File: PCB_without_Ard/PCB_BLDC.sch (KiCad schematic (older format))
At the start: 72 parts, among them J1 Ground Terminal, J2 Conn_01x03, J3 Conn_01x05, J4 Conn_01x02, J5 Conn_01x04, J6 Conn_01x04, J7 Conn_01x04, J8 Power Terminal, J9 Conn_01x02, Q1 IRF4905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

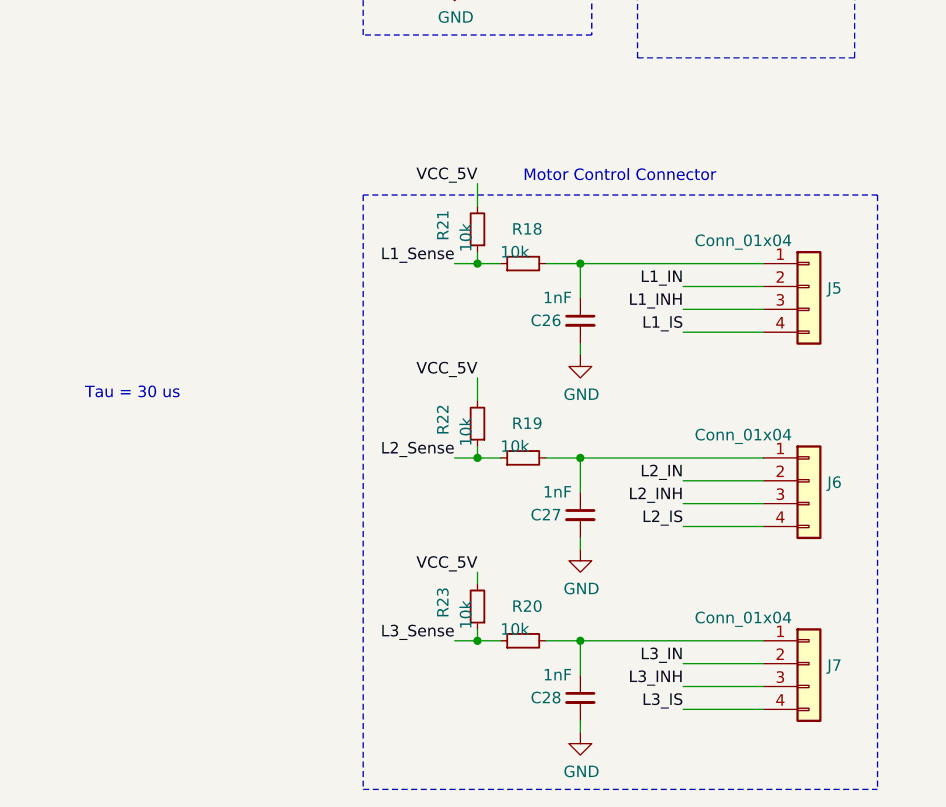
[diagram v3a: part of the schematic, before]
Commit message: Remove RC-Filter for Hall Sensors
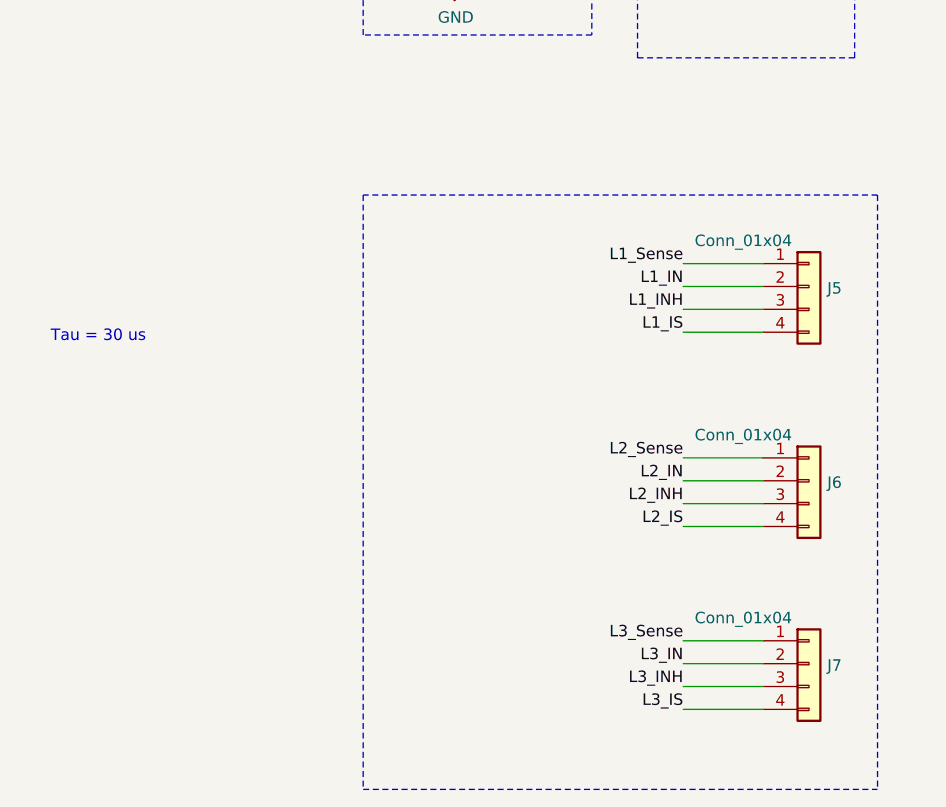
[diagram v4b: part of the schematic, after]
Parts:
- removed C26, C27, C28: 1nF, Capacitor_SMD:C_1206_3216Metric_Pad1.33x1.80mm_HandSolder, symbol Device:C_Small
- removed R18, R19, R20, R21, R22, R23: 10k, Resistor_SMD:R_1206_3216Metric_Pad1.30x1.75mm_HandSolder, symbol Device:R_Small
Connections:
- net L1_Sense: now also J5.1 (Pin_1)
- net L2_Sense: now also J6.1 (Pin_1)
- net L3_Sense: now also J7.1 (Pin_1)
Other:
- note removed: "Motor Control Connector\n"
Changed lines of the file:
@@
 Text Label 5900 4700 2    50   ~ 0
 Rot_A_Pull_Up
-Text Label 950  6300 2    50   ~ 0
-L2_Sense
 $Comp
 L power:PWR_FLAG #FLG0103
@@
 Wire Wire Line
 	6300 3650 6350 3650
-Wire Wire Line
-	1350 5450 1500 5450
-Wire Wire Line
-	1500 5800 1500 5850
-$Comp
-L power:GND #PWR05
-U 1 1 619312B0
-P 1500 5850
-F 0 "#PWR05" H 1500 5600 50  0001 C CNN
-F 1 "GND" H 1505 5677 50  0000 C CNN
-F 2 "" H 1500 5850 50  0001 C CNN
-F 3 "" H 1500 5850 50  0001 C CNN
-	1    1500 5850
-	1    0    0    -1
-$EndComp
-Wire Wire Line
-	1500 5450 1500 5600
-$Comp
-L Device:C_Small C26
-U 1 1 61C35583
-P 1500 5700
-F 0 "C26" H 1350 5700 50  0000 C CNN
-F 1 "1nF" H 1400 5800 50  0000 C CNN
-F 2 "Capacitor_SMD:C_1206_3216Metric_Pad1.33x1.80mm_HandSolder" H 1500 5700 50  0001 C CNN
-F 3 "~" H 1500 5700 50  0001 C CNN
-	1    1500 5700
-	1    0    0    -1
-$EndComp
-$Comp
-L Device:R_Small R18
-U 1 1 61C3557D
-P 1250 5450
-F 0 "R18" V 1400 5500 50  0000 R CNN
-F 1 "10k" V 1300 5550 50  0000 R CNN
-F 2 "Resistor_SMD:R_1206_3216Metric_Pad1.30x1.75mm_HandSolder" H 1250 5450 50  0001 C CNN
-F 3 "~" H 1250 5450 50  0001 C CNN
-	1    1250 5450
-	0    -1   -1   0
-$EndComp
-Text Label 950  5450 2    50   ~ 0
+Text Label 1950 5450 2    50   ~ 0
 L1_Sense
-Wire Wire Line
-	1350 7100 1500 7100
-Wire Wire Line
-	1500 7450 1500 7500
-$Comp
-L power:GND #PWR07
-U 1 1 6197CE62
-P 1500 7500
-F 0 "#PWR07" H 1500 7250 50  0001 C CNN
-F 1 "GND" H 1505 7327 50  0000 C CNN
-F 2 "" H 1500 7500 50  0001 C CNN
-F 3 "" H 1500 7500 50  0001 C CNN
-	1    1500 7500
-	1    0    0    -1
-$EndComp
-Wire Wire Line
-	1500 7100 1500 7250
-$Comp
-L Device:C_Small C28
-U 1 1 6197CE69
-P 1500 7350
-F 0 "C28" H 1350 7350 50  0000 C CNN
-F 1 "1nF" H 1400 7450 50  0000 C CNN
-F 2 "Capacitor_SMD:C_1206_3216Metric_Pad1.33x1.80mm_HandSolder" H 1500 7350 50  0001 C CNN
-F 3 "~" H 1500 7350 50  0001 C CNN
-	1    1500 7350
-	1    0    0    -1
-$EndComp
-$Comp
-L Device:R_Small R20
-U 1 1 6197CE6F
-P 1250 7100
-F 0 "R20" V 1400 7150 50  0000 R CNN
-F 1 "10k" V 1300 7200 50  0000 R CNN
-F 2 "Resistor_SMD:R_1206_3216Metric_Pad1.30x1.75mm_HandSolder" H 1250 7100 50  0001 C CNN
-F 3 "~" H 1250 7100 50  0001 C CNN
-	1    1250 7100
-	0    -1   -1   0
-$EndComp
-Text Label 950  7100 2    50   ~ 0
-L3_Sense
-Connection ~ 1500 5450
-Connection ~ 1500 7100
-Wire Wire Line
-	1350 6300 1500 6300
-Wire Wire Line
-	950  6300 1050 6300
-Wire Wire Line
-	1500 6650 1500 6700
-$Comp
-L power:GND #PWR06
-U 1 1 61A01316
-P 1500 6700
-F 0 "#PWR06" H 1500 6450 50  0001 C CNN
-F 1 "GND" H 1505 6527 50  0000 C CNN
-F 2 "" H 1500 6700 50  0001 C CNN
-F 3 "" H 1500 6700 50  0001 C CNN
-	1    1500 6700
-	1    0    0    -1
-$EndComp
-Wire Wire Line
-	1500 6300 1500 6450
-$Comp
-L Device:C_Small C27
-U 1 1 61A0131D
-P 1500 6550
-F 0 "C27" H 1350 6550 50  0000 C CNN
-F 1 "1nF" H 1400 6650 50  0000 C CNN
-F 2 "Capacitor_SMD:C_1206_3216Metric_Pad1.33x1.80mm_HandSolder" H 1500 6550 50  0001 C CNN
-F 3 "~" H 1500 6550 50  0001 C CNN
-	1    1500 6550
-	1    0    0    -1
-$EndComp
-$Comp
-L Device:R_Small R19
-U 1 1 61A01323
-P 1250 6300
-F 0 "R19" V 1400 6350 50  0000 R CNN
-F 1 "10k" V 1300 6400 50  0000 R CNN
-F 2 "Resistor_SMD:R_1206_3216Metric_Pad1.30x1.75mm_HandSolder" H 1250 6300 50  0001 C CNN
-F 3 "~" H 1250 6300 50  0001 C CNN
-	1    1250 6300
-	0    -1   -1   0
-$EndComp
-Connection ~ 1500 6300
-Text Notes -250 6050 2    50   ~ 0
+Text Notes -400 5800 2    50   ~ 0
 Tau = 30 us
 Text Notes 5000 4200 0    50   ~ 0
@@
 Text Notes 800  2550 0    50   ~ 0
 Power Terminal\n
-Wire Notes Line
-	2800 5150 550  5150
 Wire Notes Line
 	550  5150 550  7750
@@
 VCC_5V
 Wire Wire Line
-	1050 6250 1050 6300
-Connection ~ 1050 6300
-Wire Wire Line
-	1050 6300 1150 6300
-Wire Wire Line
-	1500 7100 2300 7100
-Wire Wire Line
-	1050 6800 1050 6850
-Text Label 1050 6800 2    50   ~ 0
-VCC_5V
-$Comp
-L Device:R_Small R23
-U 1 1 61975DAD
-P 1050 6950
-F 0 "R23" V 1200 7000 50  0000 R CNN
-F 1 "10k" V 1100 7050 50  0000 R CNN
-F 2 "Resistor_SMD:R_1206_3216Metric_Pad1.30x1.75mm_HandSolder" H 1050 6950 50  0001 C CNN
-F 3 "~" H 1050 6950 50  0001 C CNN
-	1    1050 6950
-	-1   0    0    1
-$EndComp
-Wire Wire Line
-	1050 7100 1150 7100
-Wire Wire Line
-	950  7100 1050 7100
-Connection ~ 1050 7100
-Wire Wire Line
-	1050 7050 1050 7100
-Wire Wire Line
-	1500 6300 2300 6300
-Text Label 1050 5950 2    50   ~ 0
-VCC_5V
-Wire Wire Line
-	1050 6050 1050 5950
-$Comp
-L Device:R_Small R22
-U 1 1 61952AAA
-P 1050 6150
-F 0 "R22" V 1200 6200 50  0000 R CNN
-F 1 "10k" V 1100 6250 50  0000 R CNN
-F 2 "Resistor_SMD:R_1206_3216Metric_Pad1.30x1.75mm_HandSolder" H 1050 6150 50  0001 C CNN
-F 3 "~" H 1050 6150 50  0001 C CNN
-	1    1050 6150
-	-1   0    0    1
-$EndComp
-Text Notes 1250 5100 0    50   ~ 0
-Motor Control Connector\n
-Text Label 1050 5100 2    50   ~ 0
-VCC_5V
-Wire Wire Line
-	1500 5450 2300 5450
-Wire Wire Line
-	1050 5100 1050 5200
-Wire Wire Line
-	1050 5450 1150 5450
-Wire Wire Line
-	950  5450 1050 5450
-Connection ~ 1050 5450
-Wire Wire Line
-	1050 5400 1050 5450
-$Comp
-L Device:R_Small R21
-U 1 1 6192D640
-P 1050 5300
-F 0 "R21" V 1200 5350 50  0000 R CNN
-F 1 "10k" V 1100 5400 50  0000 R CNN
-F 2 "Resistor_SMD:R_1206_3216Metric_Pad1.30x1.75mm_HandSolder" H 1050 5300 50  0001 C CNN
-F 3 "~" H 1050 5300 50  0001 C CNN
-	1    1050 5300
-	-1   0    0    1
-$EndComp
+	1950 5450 2300 5450
+Wire Notes Line
+	2800 5150 550  5150
+Text Label 1950 7100 2    50   ~ 0
+L3_Sense
+Text Label 1950 6300 2    50   ~ 0
+L2_Sense
+Wire Wire Line
+	1950 6300 2300 6300
+Wire Wire Line
+	1950 7100 2300 7100
 $EndSCHEMATC
